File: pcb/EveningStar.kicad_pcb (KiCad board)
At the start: 2 copper layers, 107 x 97.2 mm, 153 parts, among them J2 DEBUG, P1 WJ15EDGRC-3.81-2P, Q1 2N7002, U1 78L05G, U11 15uH, U3 ISO6721RBDR, U5 74HC14D, U6 LMR38020SDDAR, U7 ESP32-C6-WROOM-1-N8, U8 GD5F2GM7UEYIGR, U9 W5500, X1 32.768kHz, Y1 25MHz

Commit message: pcb(mb_frontend): fix drc silk clearance warnings
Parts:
- RJ2: footprint EasyEDA:RJ45-TH_RRCH-5201-6P6C -> custom:RJ45-TH_RRCH-5201-6P6C
- TP21, TP22, TP24, TP27, TP28, TP29: footprint TestPoint:TestPoint_Pad_D1.0mm -> custom:TestPoint_Pad_D1.0mm
- TP25, TP26: footprint TestPoint:TestPoint_Plated_Hole_D2.0mm -> custom:TestPoint_Plated_Hole_D2.0mm
- U1: footprint PCM_JLCPCB:SOT-89-3_L4.5-W2.5-P1.50-LS4.2-BR -> custom:SOT-89-3_L4.5-W2.5-P1.50-LS4.2-BR
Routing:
- net Net-(Q1-D): track 0.00 -> 1.86 mm
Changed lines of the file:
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@@
 		)
 	)
-	(footprint "TestPoint:TestPoint_Plated_Hole_D2.0mm"
+	(footprint "custom:TestPoint_Plated_Hole_D2.0mm"
 		(layer "F.Cu")
 		(at 57.6 67.8)
@@
 		(fp_circle
 			(center 0 0)
-			(end 0 -1.7)
+			(end 0 -1.8)
 			(stroke
 				(width 0.12)
@@
 		)
 	)
-	(footprint "TestPoint:TestPoint_Plated_Hole_D2.0mm"
+	(footprint "custom:TestPoint_Plated_Hole_D2.0mm"
 		(layer "F.Cu")
 		(at 51.05 73.905)
@@
 		)
 		(property "Value" "BAT"
-			(at 2.4 -2 0)
+			(at 2.55 -2.105 0)
 			(layer "F.SilkS")
 			(effects
@@
 		(fp_circle
 			(center 0 0)
-			(end 0 -1.7)
+			(end 0 -1.8)
 			(stroke
 				(width 0.12)
@@
 		)
 	)
-	(footprint "TestPoint:TestPoint_Pad_D1.0mm"
+	(footprint "custom:TestPoint_Pad_D1.0mm"
 		(layer "F.Cu")
 		(at 64.7 63.55)
@@
 		)
 		(property "Value" "RX_ISO"
-			(at -0.5 -3.75 270)
+			(at -0.5 -3.55 90)
 			(layer "F.SilkS")
 			(effects
@@
 		(fp_circle
 			(center 0 0)
-			(end 0 0.7)
+			(end 0 0.8)
 			(stroke
 				(width 0.12)
@@
 		)
 	)
-	(footprint "TestPoint:TestPoint_Pad_D1.0mm"
+	(footprint "custom:TestPoint_Pad_D1.0mm"
 		(layer "F.Cu")
 		(at 99.375 62.92)
@@
 			(at 0 -1.448 0)
 			(layer "F.SilkS")
+			(hide yes)
 			(effects
 				(font
@@
 		)
 		(property "Value" "WRITE"
-			(at 0 1.55 0)
-			(layer "F.Fab")
+			(at -2.5 -0.25 0)
+			(layer "F.SilkS")
 			(effects
 				(font
@@
 		(fp_circle
 			(center 0 0)
-			(end 0 0.7)
+			(end 0 0.8)
 			(stroke
 				(width 0.12)
@@
 		)
 	)
-	(footprint "PCM_JLCPCB:SOT-89-3_L4.5-W2.5-P1.50-LS4.2-BR"
+	(footprint "custom:SOT-89-3_L4.5-W2.5-P1.50-LS4.2-BR"
 		(layer "F.Cu")
 		(at 62.45 51.41 90)
@@
 		)
 		(fp_circle
-			(center 1 2)
-			(end 1.03 2)
+			(center 1.5 2.5)
+			(end 1.53 2.5)
 			(stroke
 				(width 0.15)
@@
 		)
 	)
-	(footprint "TestPoint:TestPoint_Pad_D1.0mm"
+	(footprint "custom:TestPoint_Pad_D1.0mm"
 		(layer "F.Cu")
 		(at 66.475 49.325)
@@
 		)
 		(property "Value" "VCC_ISO"
-			(at -2.25 -1.75 180)
+			(at -1.475 -1.925 0)
 			(layer "F.SilkS")
 			(effects
@@
 		(fp_circle
 			(center 0 0)
-			(end 0 0.7)
+			(end 0 0.8)
 			(stroke
 				(width 0.12)
@@
 		)
 	)
-	(footprint "EasyEDA:RJ45-TH_RRCH-5201-6P6C"
+	(footprint "custom:RJ45-TH_RRCH-5201-6P6C"
 		(layer "F.Cu")
 		(at 48.52 65.03 180)
@@
 		(sheetname "/meterbus_frontend/")
 		(sheetfile "meterbus_frontend.kicad_sch")
-		(units
-			(unit
-				(name "A")
-				(pins "1" "2" "3" "4" "5" "6")
-			)
-		)
 		(attr through_hole)
 		(duplicate_pad_numbers_are_jumpers no)
 		(fp_line
-			(start 6.73 14.04)
-			(end 6.73 -2.38)
-			(stroke
-				(width 0.25)
-				(type solid)
-			)
-			(layer "F.SilkS")
-		)
-		(fp_line
-			(start -6.51 -2.47)
-			(end 6.73 -2.41)
+			(start 7.1 14.04)
+			(end 7.1 -2.4)
 			(stroke
 				(width 0.25)
@@
 		)
 		(fp_line
-			(start -6.51 -2.47)
-			(end -6.73 -2.47)
+			(start -7.1 14.04)
+			(end 7.1 14.04)
 			(stroke
 				(width 0.25)
@@
 		)
 		(fp_line
-			(start -6.73 14.04)
-			(end 6.73 14.04)
+			(start -7.1 -2.4)
+			(end -7.1 14.04)
 			(stroke
 				(width 0.25)
@@
 		)
 		(fp_line
-			(start -6.73 -2.47)
-			(end -6.73 14.04)
+			(start -7.1 -2.41)
+			(end 7.1 -2.41)
 			(stroke
 				(width 0.25)
@@
 		)
 		(fp_circle
-			(center -6.73 -2.45)
-			(end -6.7 -2.45)
-			(stroke
-				(width 0.06)
-				(type solid)
-			)
-			(fill no)
-			(layer "F.SilkS")
-		)
-		(fp_circle
 			(center 5.08 7.62)
 			(end 5.78 7.62)
@@
 			)
 		)
-		(pad "" thru_hole circle
+		(pad "" np_thru_hole circle
 			(at -5.08 7.62 180)
 			(size 3.3 3.3)
 			(drill 3.3)
 			(layers "*.Cu" "*.Mask")
-			(remove_unused_layers no)
 		)
-		(pad "" thru_hole circle
+		(pad "" np_thru_hole circle
 			(at 5.08 7.62 180)
 			(size 3.3 3.3)
 			(drill 3.3)
 			(layers "*.Cu" "*.Mask")
-			(remove_unused_layers no)
 		)
 		(pad "1" thru_hole rect
@@
 		(sheetname "/meterbus_frontend/")
 		(sheetfile "meterbus_frontend.kicad_sch")
+		(units
+			(unit
+				(name "A")
+				(pins "1" "2")
+			)
+		)
 		(attr through_hole)
 		(duplicate_pad_numbers_are_jumpers no)
@@
 		(embedded_fonts no)
 	)
-	(footprint "TestPoint:TestPoint_Pad_D1.0mm"
+	(footprint "custom:TestPoint_Pad_D1.0mm"
 		(layer "F.Cu")
 		(at 93.375 62.67)
@@
 			(at 0 -1.448 0)
 			(layer "F.SilkS")
+			(hide yes)
 			(effects
 				(font
@@
 		)
 		(property "Value" "READ"
-			(at 0 1.55 0)
-			(layer "F.Fab")
+			(at -2.5 -0.25 0)
+			(layer "F.SilkS")
 			(effects
 				(font
@@
 		(fp_circle
 			(center 0 0)
-			(end 0 0.7)
+			(end 0 0.8)
 			(stroke
 				(width 0.12)
@@
 		)
 	)
-	(footprint "TestPoint:TestPoint_Pad_D1.0mm"
+	(footprint "custom:TestPoint_Pad_D1.0mm"
 		(layer "F.Cu")
 		(at 58.45 74.505)
@@
 		(fp_circle
 			(center 0 0)
-			(end 0 0.7)
+			(end 0 0.8)
 			(stroke
 				(width 0.12)
@@
 		(embedded_fonts no)
 	)
-	(footprint "TestPoint:TestPoint_Pad_D1.0mm"
+	(footprint "custom:TestPoint_Pad_D1.0mm"
 		(layer "F.Cu")
 		(at 64.6 65.6)
@@
 		)
 		(property "Value" "TX_ISO"
-			(at 0.2 1.6 180)
+			(at 0.8 1.8 0)
 			(layer "F.SilkS")
 			(effects
@@
 		(fp_circle
 			(center 0 0)
-			(end 0 0.7)
+			(end 0 0.8)
 			(stroke
 				(width 0.12)
@@
 	)
 	(segment
+		(start 61.03 72.305)
+		(end 59.45 72.305)
+		(width 0.2)
+		(layer "F.Cu")
+		(net "Net-(Q1-D)")
+	)
+	(segment
+		(start 59.45 72.305)
+		(end 59.25 72.505)
+		(width 0.2)
+		(layer "F.Cu")
+		(net "Net-(Q1-D)")
+	)
+	(segment

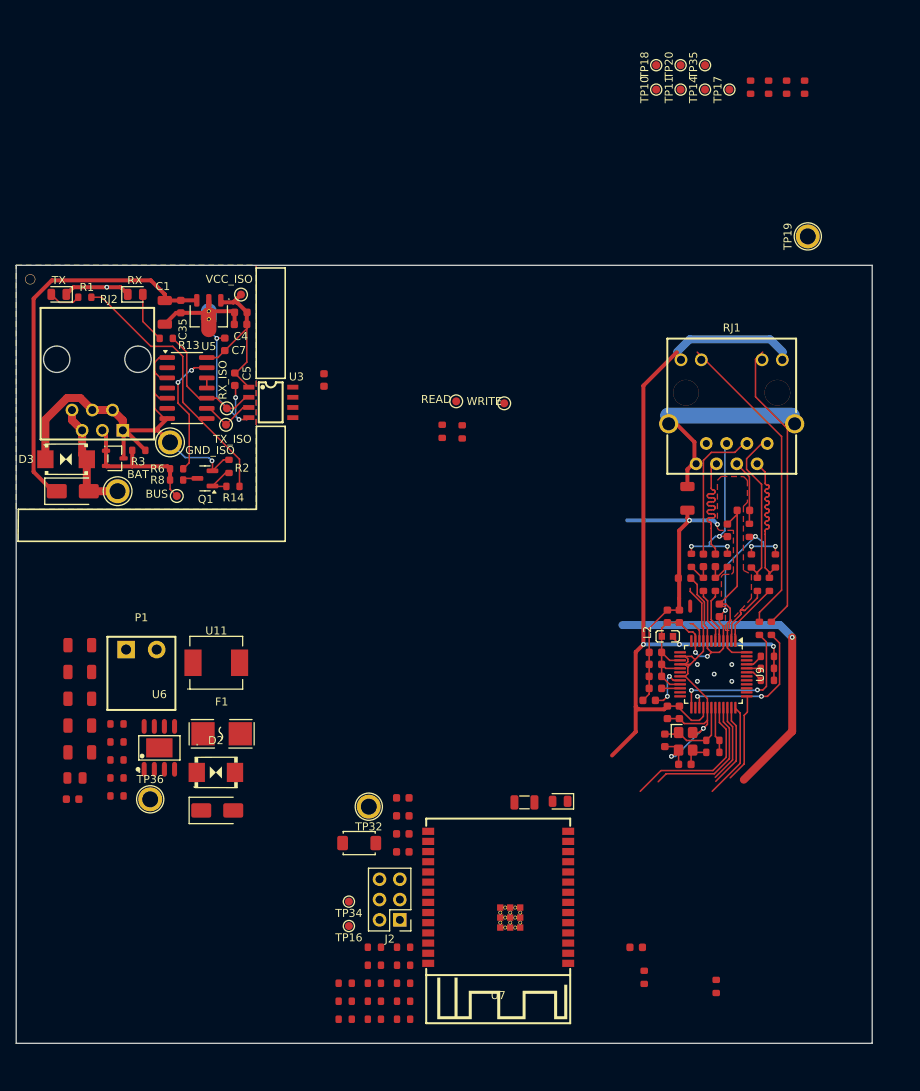
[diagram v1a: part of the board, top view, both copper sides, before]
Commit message: pcb(eth): layout w5500
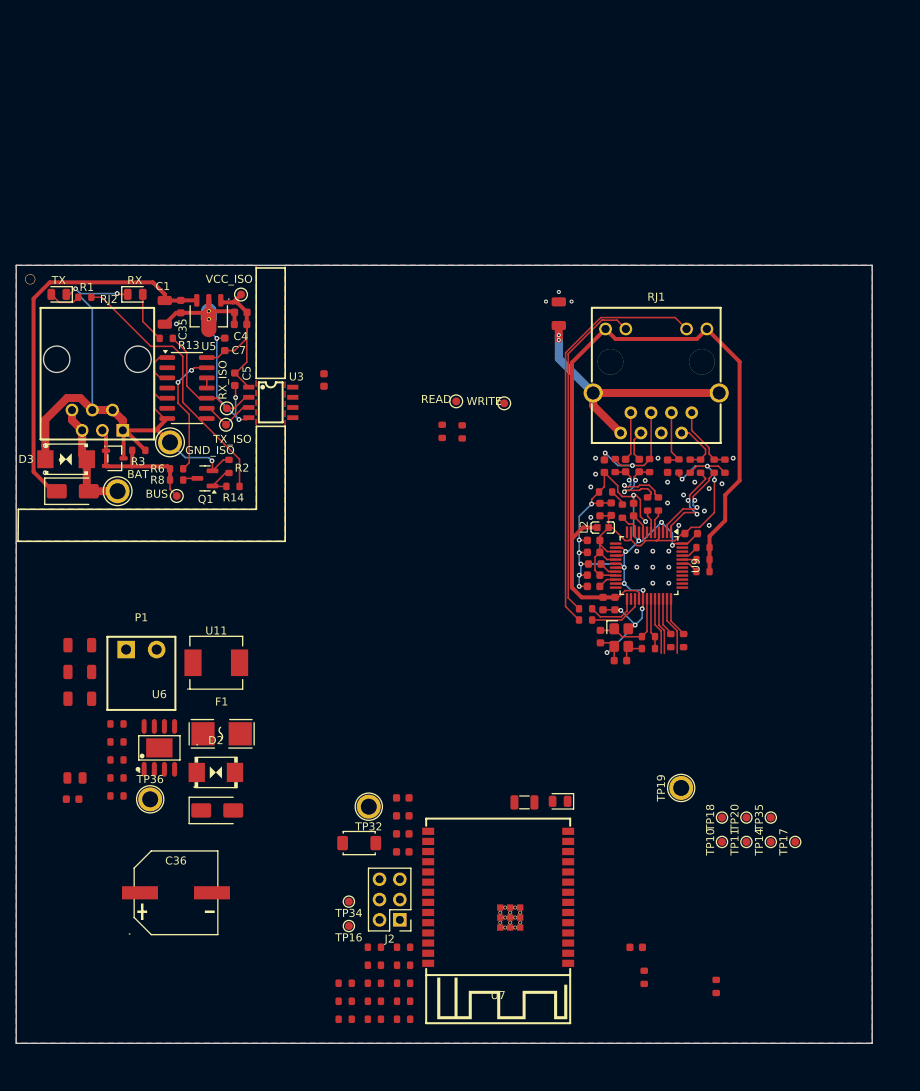
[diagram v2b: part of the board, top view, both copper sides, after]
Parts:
- removed C42, C43: 4.7uF, PCM_JLCPCB:C_1206
- added C36: 22uF 160V, EasyEDA:CAP-SMD_BD10.0-L10.3-W10.3-FD, F.Cu at (58.4, 124.1)
- moved TP10 94.4 mm to (126.6, 117.8)
- moved TP11 94.4 mm to (129.7, 117.8)
- moved TP14 94.4 mm to (132.7, 117.8)
- moved TP17 94.4 mm to (135.8, 117.8)
- moved TP18 94.4 mm to (126.6, 114.7)
- moved TP20 94.4 mm to (129.7, 114.7)
- moved TP35 94.4 mm to (132.7, 114.7)
- moved TP19 70.7 mm to (121.5, 111.0)
- moved R50 70.4 mm to (121.8, 92.6)
- moved R37 70.2 mm to (120.2, 92.6)
- moved R52 56.4 mm to (112.0, 74.0), turned to 0 degrees
- moved R4 55.4 mm to (114.2, 76.4)
- moved C21 28.1 mm to (106.2, 51.7), turned to -90 degrees
- moved R47 23.2 mm to (109.5, 90.0), turned to 0 degrees
- moved R46 21.9 mm to (109.5, 88.6), turned to 0 degrees
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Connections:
- net Net-(C31-Pad1) renamed /ethernet/RDMID+
- net Net-(C32-Pad1) renamed /ethernet/RDMID-
- RJ1 pad 13: (no net) -> CGND
- RJ1 pad 14: (no net) -> CGND
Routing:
- net (no net): track 43.3 -> 0.00 mm, vias 1 -> 0
- net Net-(R47-Pad1): track 36.6 -> 51.6 mm
- net GND_ISO: track 98.2 -> 113.2 mm, vias 5 -> 10
- net /ethernet/RD+: track 17.9 -> 3.90 mm
- net /ethernet/TD-: track 20.5 -> 6.69 mm
- net GND: track 108.1 -> 95.7 mm, vias 9 -> 46
- net /ethernet/TD+: track 20.7 -> 8.38 mm
- net /ethernet/ACT_LED: track 19.1 -> 7.02 mm, vias 2 -> 0
- net /ethernet/LINK_LED: track 18.6 -> 6.58 mm, vias 2 -> 0
- net /ethernet/CS: track 19.0 -> 7.05 mm
- net /ethernet/RD-: track 17.8 -> 6.10 mm
- net /mcu/ETH_RST: track 11.1 -> 0.00 mm
- net /ethernet/SCK: track 16.7 -> 7.00 mm
- net Net-(U9-~{INT}): track 12.1 -> 5.06 mm
- net CGND: track 26.1 -> 32.7 mm, vias 0 -> 2
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- added copper zone on B.Cu, net GND

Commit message: pcb(eth): fix some drc errors
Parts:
- TP10, TP11, TP14, TP17, TP18, TP20, TP35: footprint TestPoint:TestPoint_Pad_D1.0mm -> custom:TestPoint_Pad_D1.0mm
- TP19: footprint TestPoint:TestPoint_Plated_Hole_D2.0mm -> custom:TestPoint_Plated_Hole_D2.0mm
- moved TP35 40.4 mm to (125.0, 75.0)
- moved TP14 25.9 mm to (118.4, 96.2)
- moved TP17 25.6 mm to (122.0, 96.2)
- moved TP10 22.7 mm to (116.6, 97.4)
- moved TP19 22.4 mm to (124.6, 88.8)
- moved TP11 22.2 mm to (125.4, 96.0)
- moved TP20 19.7 mm to (120.2, 97.4)
- moved TP18 17.5 mm to (123.8, 97.4)
- moved C20 0.23 mm to (113.0, 88.0)
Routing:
- net /mcu/ETH_RST: track 0.00 -> 11.8 mm
- net /ethernet/INT: track 0.00 -> 4.83 mm
- net /ethernet/CS: track 7.05 -> 11.3 mm
- net /ethernet/MISO: track 0.00 -> 4.00 mm
- net /ethernet/SCK: track 7.00 -> 9.44 mm
- net /ethernet/MOSI: track 7.25 -> 9.69 mm
- net +3V3A: track 56.4 -> 57.0 mm
- net GND: track 95.7 -> 95.1 mm

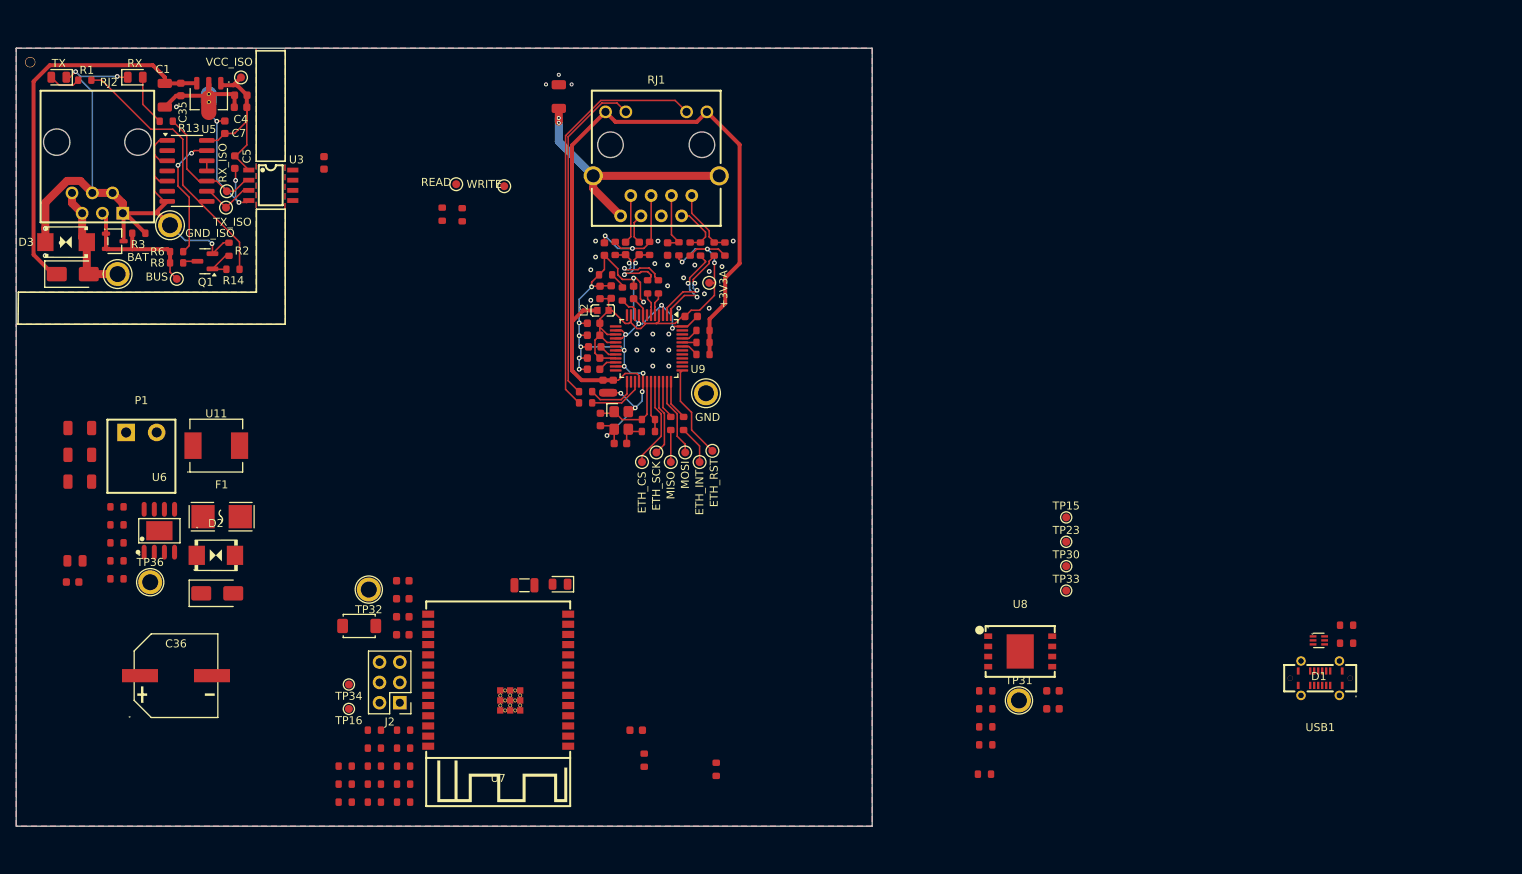
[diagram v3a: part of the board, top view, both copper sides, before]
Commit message: pcb(psu): layout dc-dc converter
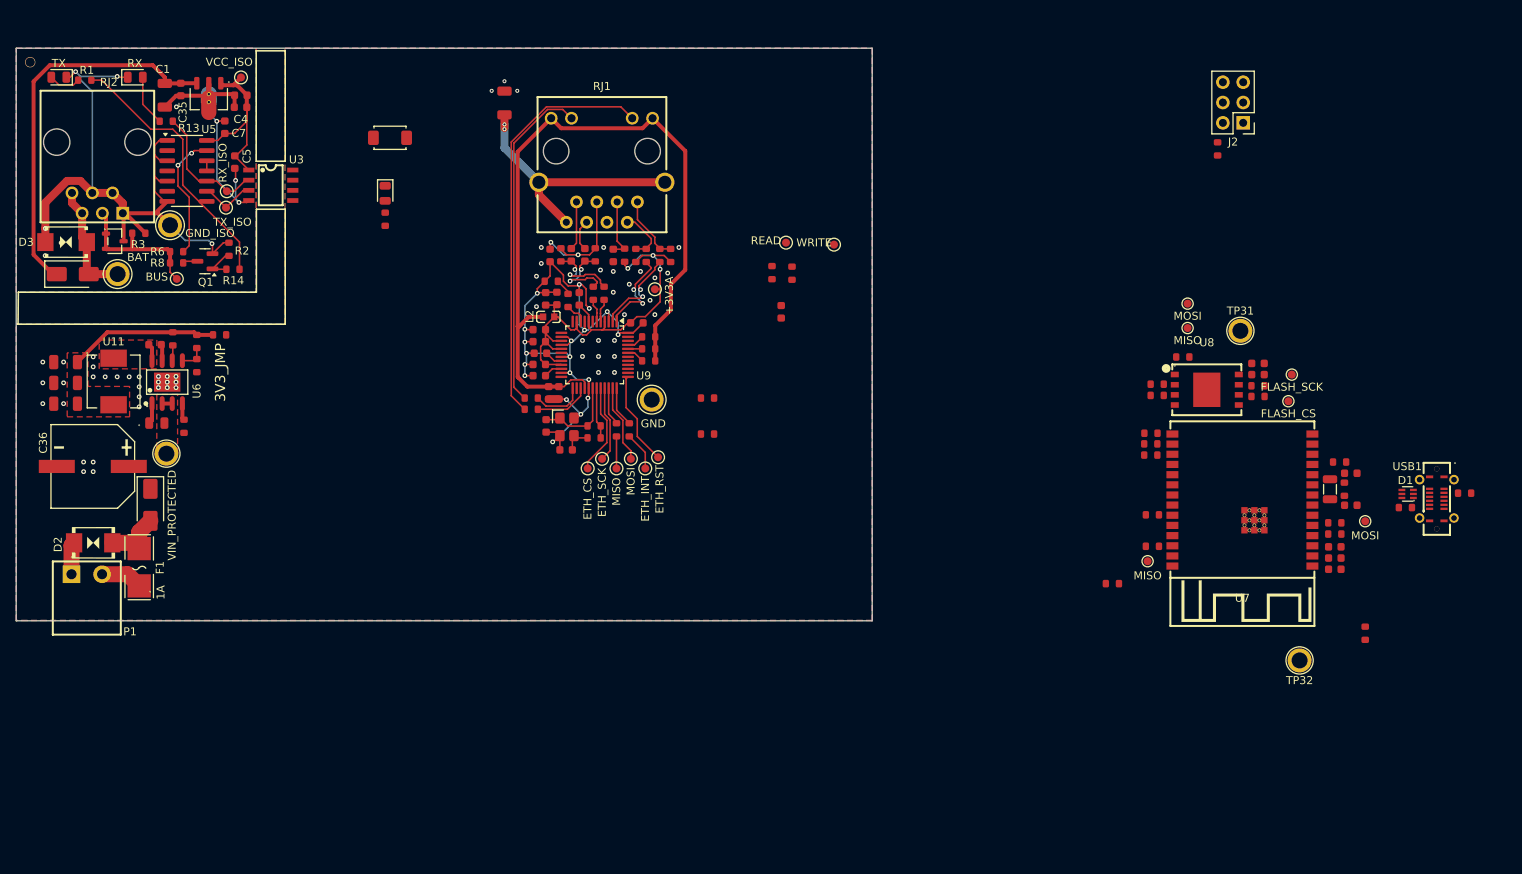
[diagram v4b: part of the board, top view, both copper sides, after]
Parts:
- moved R7 130.5 mm to (188.6, 58.3), turned to -90 degrees
- moved TP34 128.7 mm to (207.0, 104.8)
- moved J2 127.9 mm to (191.8, 55.0)
- moved R65 127.4 mm to (203.2, 105.0), turned to 0 degrees
- moved R55 124.6 mm to (203.2, 106.4), turned to 0 degrees
- moved R23 122.0 mm to (204.4, 100.8), turned to -90 degrees
- moved C11 119.5 mm to (205.2, 98.8), turned to 0 degrees
- moved C12 118.9 mm to (205.2, 102.8), turned to 0 degrees
- moved C2 117.0 mm to (203.2, 108.0), turned to 0 degrees
- moved TP32 116.7 mm to (198.8, 122.2)
- moved C8 116.7 mm to (203.2, 110.8)
- moved R58 113.3 mm to (184.2, 84.3), turned to 0 degrees
- moved R63 109.6 mm to (180.2, 96.5)
- moved R64 105.2 mm to (180.4, 107.9)
- moved R62 103.4 mm to (180.2, 95.1)
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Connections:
- U6 pad 9: (no net) -> GND
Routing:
- net Net-(C10-Pad1): track 0.00 -> 18.6 mm
- net Net-(D2-A): track 0.00 -> 7.71 mm
- net GND: track 95.1 -> 101.7 mm, vias 46 -> 75
- net Net-(F1-Pad1): track 0.00 -> 5.24 mm
- net Net-(U6-FB): track 0.00 -> 3.26 mm
- net Net-(U6-SW): track 0.00 -> 2.17 mm
- net Net-(U6-RT/SYNC): track 0.00 -> 2.10 mm
- net Net-(U6-BOOT): track 0.00 -> 2.05 mm
- net /mcu/PGOOD: track 0.00 -> 1.94 mm
- net Net-(U6-EN): track 0.00 -> 1.26 mm
- added copper zone on F.Cu, net Net-(C10-Pad1)
- added copper zone on F.Cu, net Net-(U6-EN)
- added copper zone on F.Cu, net Net-(U6-SW)
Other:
- board size 107 x 97.2 mm -> 107 x 71.6 mm
